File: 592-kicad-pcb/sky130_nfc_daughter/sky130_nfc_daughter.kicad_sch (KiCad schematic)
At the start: 57 parts, among them J1 U.FL, J2 U.FL, J3 U.FL, J4 U.FL, J5 U.FL, J6 U.FL, J7 U.FL, U1 Caravel_QFN, U3 W25Q32JVZP

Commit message: Add files via upload
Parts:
- removed C10: 0.1uf, Capacitor_SMD:C_0402_1005Metric, symbol Device:C
- removed C15, C16, C17, C3: C_1u_0603_50V, Capacitor_SMD:C_0603_1608Metric, symbol psypassives:C_1u_0603_50V
- removed R3, R4: 0R, Resistor_SMD:R_1206_3216Metric, symbol Device:R
- added C10, C20, C21, C23: C_1u_0603_50V, Capacitor_SMD:C_0603_1608Metric, symbol psypassives:C_1u_0603_50V
- added C22, C3: 0.1uf, Capacitor_SMD:C_0402_1005Metric, symbol Device:C
- added JP10, JP11, JP6, JP7, JP8, JP9: Jumper_2_Small_Bridged, Jumper:SolderJumper-2_P1.3mm_Bridged_RoundedPad1.0x1.5mm, symbol Jumper:Jumper_2_Small_Bridged
- added R1: 10k, Resistor_SMD:R_0402_1005Metric, symbol Device:R
- added TP5: TestPoint_Alt, TestPoint:TestPoint_Keystone_5019_Minature, symbol Connector:TestPoint_Alt
- TP1, TP2, TP3, TP4: now fitted
- TP6: renamed from TP9; now fitted
- renumbered JP13 to JP2, JP2 to JP5
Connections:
- net GND: now also CON1.17 (Pin_17), C10.2, C20.2, C21.2, C22.2, C23.1, C3.1; no longer CON1.27 (Pin_27), CON1.33 (Pin_33)
- net VDD_EXT: now also C22.1, C23.2, JP11.2 (B), TP5.1; no longer CON1.39 (Pin_39)
- net ext_clk_dig: now also J3.1, JP5.1 (A)
- net ext_reset_dig: no longer J3.1, JP5.1 (A)
- net flash_csb: now also R1.2
- net gpio_0_0: now also CON1.19 (Pin_19)
- net gpio_1_0: now also CON1.21 (Pin_21)
- net at CON1.14 (Pin_14): now also JP10.1 (A)
- net flash_wpb: now reaches R9.2, U3.3 (~{WP}/IO_{2})
- net flash_rstb: now reaches R10.2, U3.7 (~{HOLD}/~{RESET}/IO_{3})
- net vccd_all renamed vccd_user_1v8
- net vccd_user_1v8: now also TP3.1, JP9.1 (A); no longer C2.1, C4.2, TP2.1, U1.18 (vccd)
- net vccd_in: no longer names the net of CON1.7 (Pin_7)
- net vccd_in: no longer TP4.1
- net vdda_all renamed vdda_user_3v3
- net vdda_user_3v3: now also TP4.1, C20.1, C21.1, JP10.2 (B), JP8.1 (A); no longer R10.1, R9.1, TP1.1, U1.30 (vdda), U3.8 (VCC)
- net vdda_in: no longer names the net of CON2.2 (Pin_2)
- net vdda_in: now also JP6.1 (A); no longer TP3.1
- net vddio renamed vddio_vdda_mgmt_3v3
- net vddio_vdda_mgmt_3v3: now also R10.1, R9.1, TP2.1, U1.30 (vdda), U3.8 (VCC), C3.2, JP7.2 (B), R1.1; no longer CON2.4 (Pin_4)
- new net: CON1.27 (Pin_27), JP8.2 (B)
- new net: CON1.33 (Pin_33), JP9.2 (B)
- new net: CON1.39 (Pin_39), JP11.1 (A)
- new net: CON2.4 (Pin_4), JP7.1 (A)
- new net vccd_mgmt_1v8: C10.1, C2.1, C4.2, JP6.2 (B), TP1.1, U1.18 (vccd)
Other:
- note added: "ADD RESET BUTTON"
- note added: "PWR/GND probes"
- note removed: "Bidir[0..1]"
- note removed: "GND probe point"
- note removed: "Input (7 below)"
- note removed: "Replace 0R with current sense resistors to monitor current on rail"
- moved on the sheet: C1, C11, C12, C13, C14, C18, C19, C4, C5, C6, C7, C8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

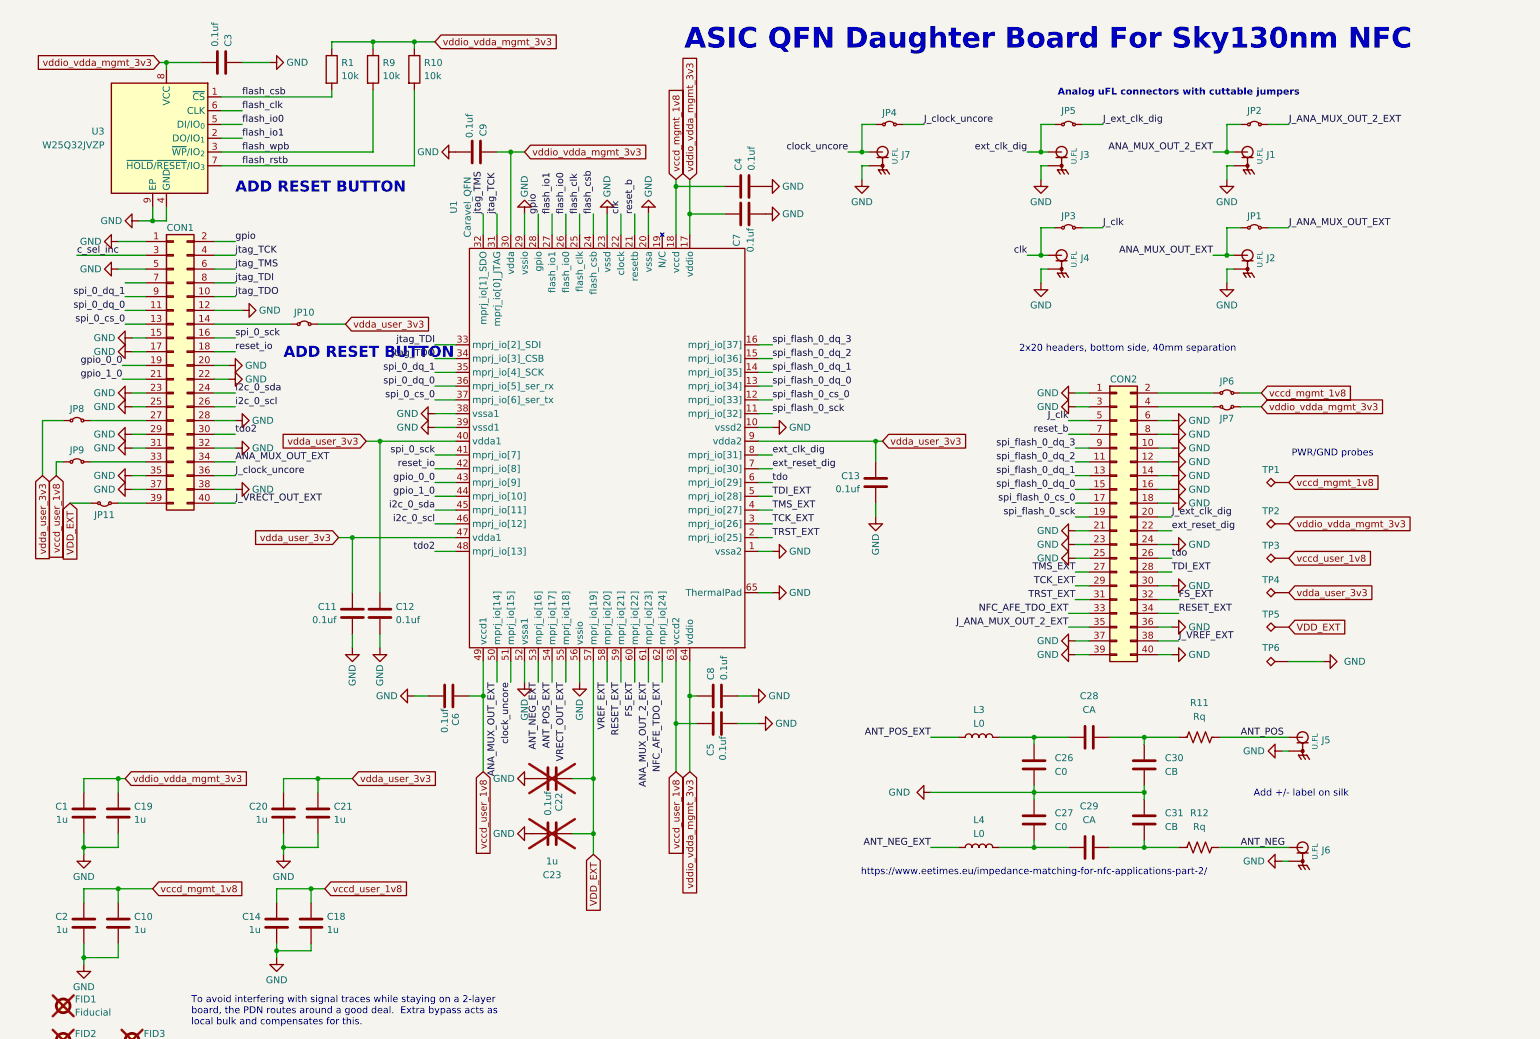
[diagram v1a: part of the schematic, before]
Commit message: add mezzanine symbol/footprint, init daughterboard placement
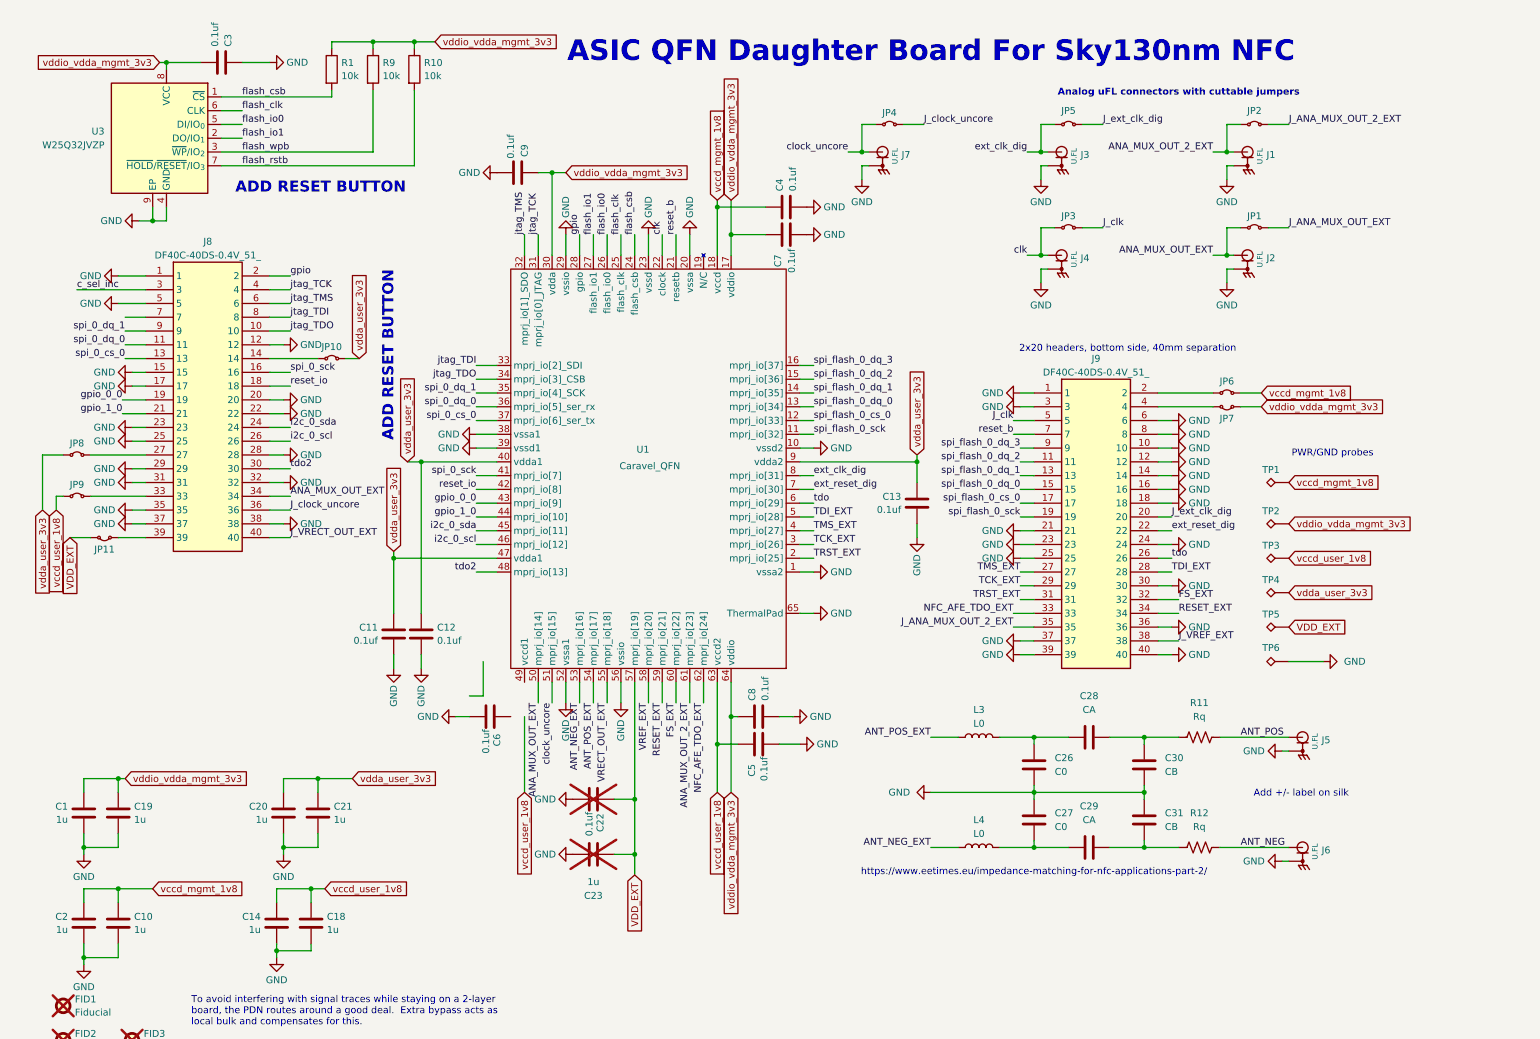
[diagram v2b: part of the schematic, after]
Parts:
- removed CON1, CON2: ~, TinyTapeout:FH-00148_PinSocket_2x20_P2.54mm, symbol Connector_Generic:Conn_02x20_Odd_Even
- added J8, J9: DF40C-40DS-0.4V_51_, 592-partslib:DF40C40DS04V51, symbol 592-partslib:DF40C-40DS-0.4V_51_
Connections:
- net ANA_MUX_OUT_EXT: now also J8.34
- net FS_EXT: now also J9.32
- net GND: now also J8.1, J8.12, J8.15, J8.17, J8.20, J8.22, J8.23, J8.25, J8.28, J8.29, J8.31, J8.32, J8.35, J8.37, J8.38, J8.5, J9.1, J9.10, J9.12, J9.14, J9.16, J9.18, J9.21, J9.23, J9.24, J9.25, J9.3, J9.30, J9.36, J9.37, J9.39, J9.40, J9.6, J9.8
- net J_ANA_MUX_OUT_2_EXT: now also J9.35
- net J_VRECT_OUT_EXT: now also J8.40
- net J_VREF_EXT: now also J9.38
- net J_clk: now also J9.5
- net J_clock_uncore: now also J8.36
- net J_ext_clk_dig: now also J9.20
- net NFC_AFE_TDO_EXT: now also J9.33
- net RESET_EXT: now also J9.34
- net TCK_EXT: now also J9.29
- net TDI_EXT: now also J9.28
- net TMS_EXT: now also J9.27
- net TRST_EXT: now also J9.31
- net c_sel_inc: now also J8.3
- net ext_reset_dig: now also J9.22
- net gpio: now also J8.2
- net gpio_0_0: now also J8.19
- net gpio_1_0: now also J8.21
- net i2c_0_scl: now also J8.26
- net i2c_0_sda: now also J8.24
- net jtag_TCK: now also J8.4
- net jtag_TDI: now also J8.8
- net jtag_TDO: now also J8.10
- net jtag_TMS: now also J8.6
- net reset_b: now also J9.7
- net reset_io: now also J8.18
- net spi_0_cs_0: now also J8.13
- net spi_0_dq_0: now also J8.11
- net spi_0_dq_1: now also J8.9
- net spi_0_sck: now also J8.16
- net spi_flash_0_cs_0: now also J9.17
- net spi_flash_0_dq_0: now also J9.15
- net spi_flash_0_dq_1: now also J9.13
- net spi_flash_0_dq_2: now also J9.11
- net spi_flash_0_dq_3: now also J9.9
- net spi_flash_0_sck: now also J9.19
- net tdo: now also J9.26
- net tdo2: now also J8.30
- net vccd_user_1v8: no longer C6.1, U1.49 (vccd1)
- net at JP10.1 (A): now also J8.14
- net at JP8.2 (B): now also J8.27
- net at JP9.2 (B): now also J8.33
- net at JP11.1 (A): now also J8.39
- net at JP7.1 (A): now also J9.4
- net at JP6.1 (A): now also J9.2
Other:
- moved on the sheet: C11, C12, C13, C22, C23, C4, C5, C6, C7, C8, C9, JP10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

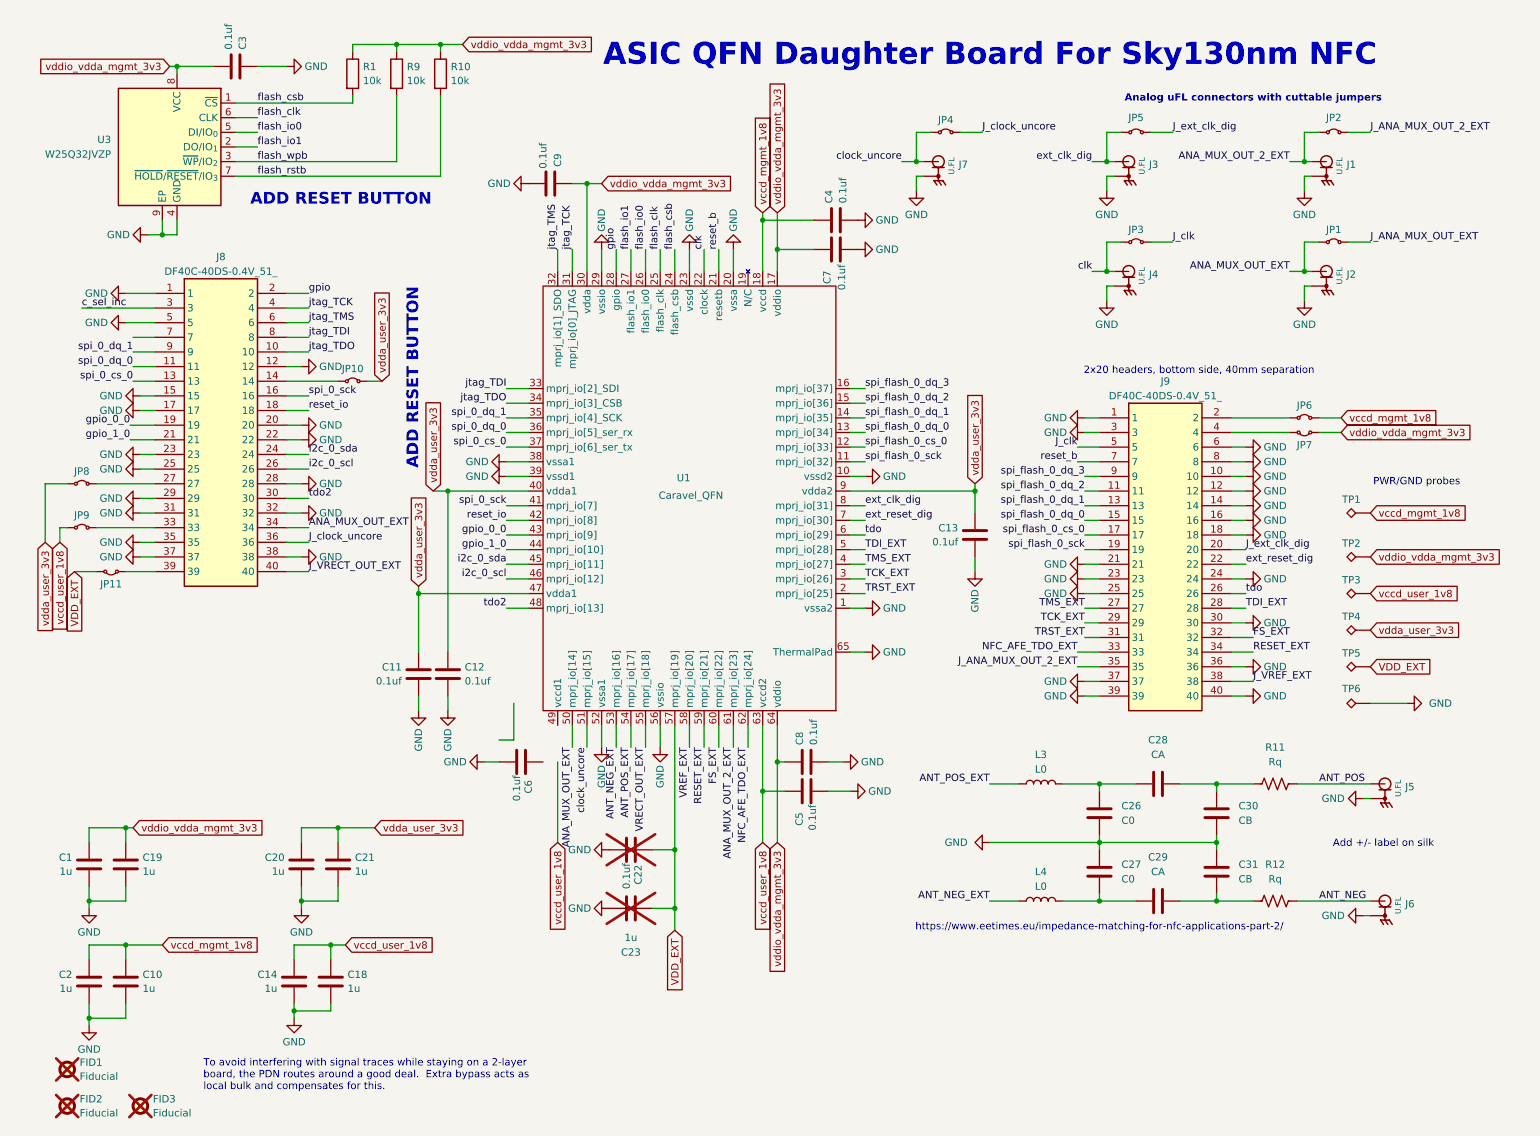
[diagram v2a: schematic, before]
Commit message: daughter placement v1, add 3D models for mezzanine + uFL
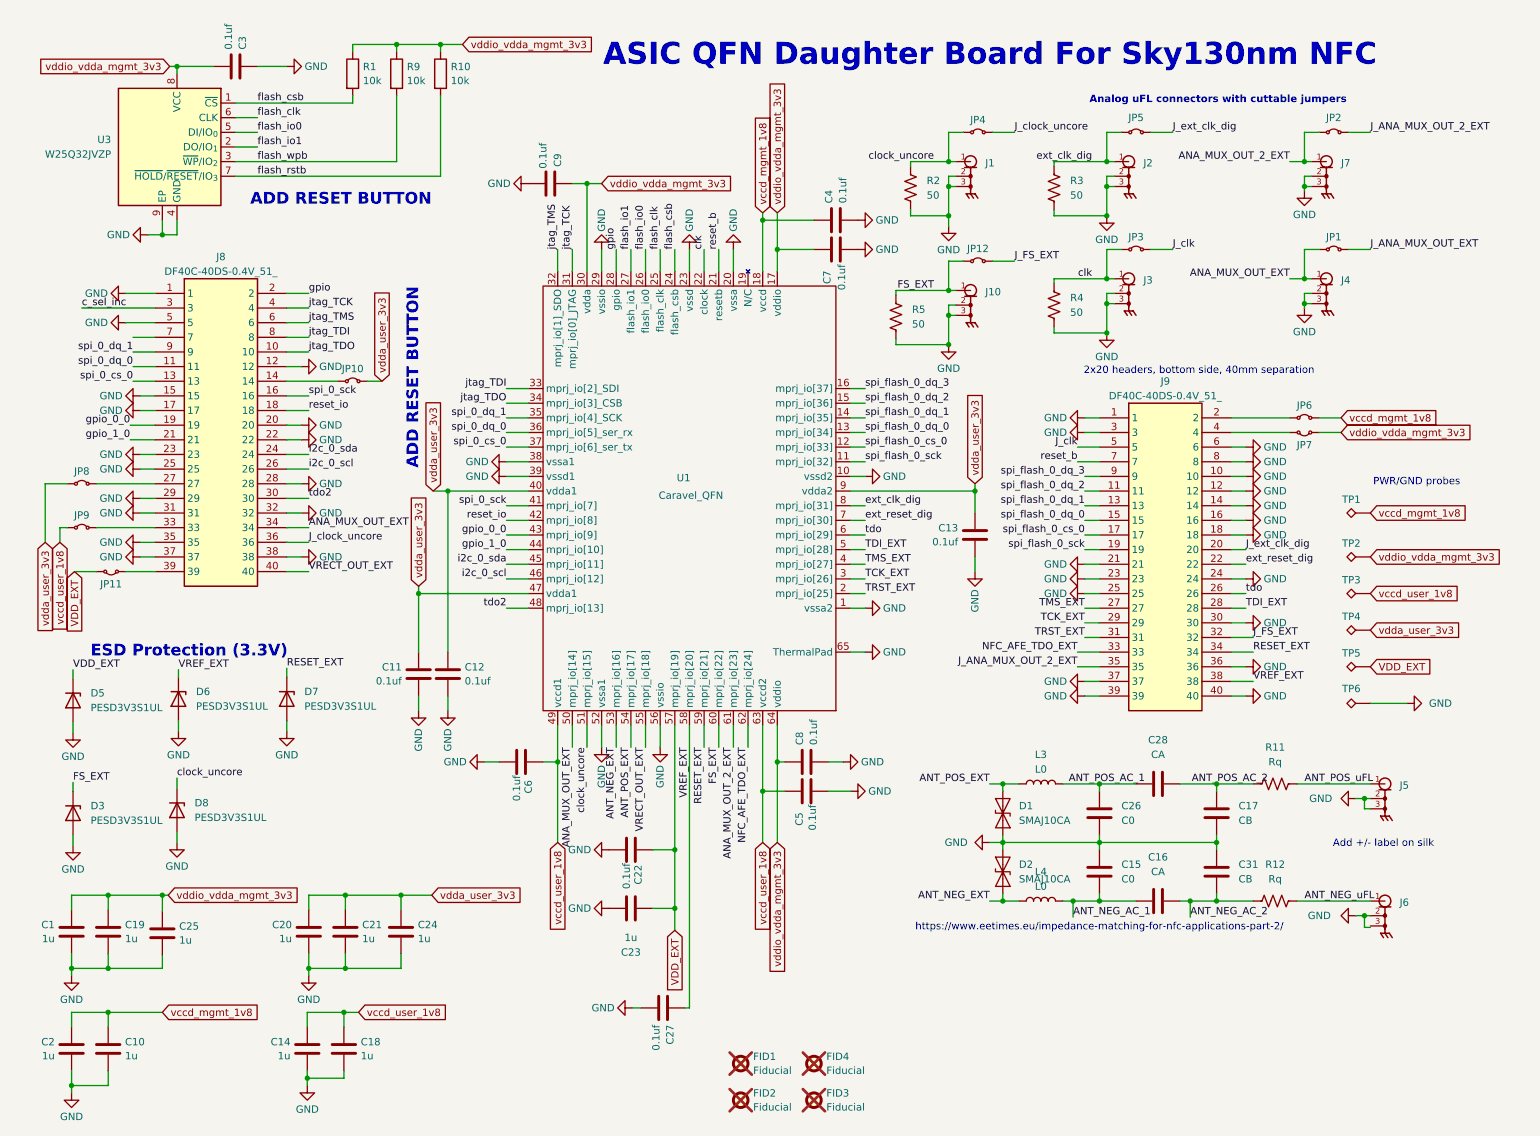
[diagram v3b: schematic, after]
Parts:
- removed C29: CA, symbol Device:C
- removed C30: CB, symbol Device:C
- removed J1, J2, J3, J4, J5, J6, J7: U.FL, psysnapeda:SAMTEC_RSP-122811-01, symbol psysnapeda:RSP-122811-01
- added C15: C0, Capacitor_SMD:C_0603_1608Metric_Pad1.08x0.95mm_HandSolder, symbol Device:C
- added C16: CA, Capacitor_SMD:C_0603_1608Metric_Pad1.08x0.95mm_HandSolder, symbol Device:C
- added C17: CB, Capacitor_SMD:C_0603_1608Metric_Pad1.08x0.95mm_HandSolder, symbol Device:C
- added C24, C25: C_1u_0603_50V, Capacitor_SMD:C_0603_1608Metric, symbol psypassives:C_1u_0603_50V
- added D1, D2: SMAJ10CA, Diode_SMD:D_SMA, symbol Diode:SMAJ10CA
- added D3, D5, D6, D7, D8: PESD3V3S1UL, Diode_SMD:D_SOD-882, symbol Diode:PESD3V3S1UL
- added FID4: Fiducial, Fiducial:Fiducial_1mm_Mask2mm, symbol Mechanical:Fiducial
- added J1, J10, J2, J3, J4, J5, J6, J7: U.FL-R-SMT-1_80_, 592-partslib:UFLRSMT180, symbol 592-partslib:U.FL-R-SMT-1_80_
- added JP12: Jumper_2_Small_Bridged, Jumper:SolderJumper-2_P1.3mm_Bridged_RoundedPad1.0x1.5mm, symbol Jumper:Jumper_2_Small_Bridged
- added R2, R3, R4, R5: 50, Resistor_SMD:R_0402_1005Metric, symbol Device:R_US
- C22, C23: now fitted
- C26, C28, C31: footprint (none) -> Capacitor_SMD:C_0603_1608Metric_Pad1.08x0.95mm_HandSolder
- C27: value C0 -> 0.1uf; footprint (none) -> Capacitor_SMD:C_0402_1005Metric; Characteristics (none) -> 100n 0402; LCSC (none) -> C100072; MPN (none) -> CL05A104KA5NNNC; MPN_ALT (none) -> GRM155R71E104KE14J
- L3, L4: footprint (none) -> Inductor_SMD:L_0603_1608Metric_Pad1.05x0.95mm_HandSolder
- R11, R12: footprint (none) -> Resistor_SMD:R_0603_1608Metric_Pad0.98x0.95mm_HandSolder
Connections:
- net J_VRECT_OUT_EXT is gone; now on net VRECT_OUT_EXT: J8.40
- net J_VREF_EXT is gone; now on net VREF_EXT: J9.38
- net ANA_MUX_OUT_2_EXT: now also J7.1
- net ANA_MUX_OUT_EXT: now also J4.1
- net ANT_NEG_EXT: now also D2.2 (A2)
- net ANT_POS_EXT: now also D1.2 (A2)
- net FS_EXT: now also D3.1 (K), J10.1, JP12.1 (A), R5.2; no longer J9.32
- net GND: now also C27.2, C15.1, C17.2, C24.2, C25.2, D1.1 (A1), D2.1 (A1), D3.2 (A), D5.2 (A), D6.2 (A), D7.2 (A), D8.2 (A), J1.2, J1.3, J10.2, J10.3, J2.2, J2.3, J3.2, J3.3, J4.2, J4.3, J5.2, J5.3, J6.2, J7.2, J7.3, R2.1, R3.1, R4.1, R5.1; no longer C27.1
- net RESET_EXT: now also D7.1 (K)
- net VDD_EXT: now also D5.1 (K)
- net VREF_EXT: now also C27.1, D6.1 (K)
- net clk: now also J3.1, R4.2
- net clock_uncore: now also D8.1 (K), J1.1, R2.2
- net ext_clk_dig: now also J2.1, R3.2
- net vccd_user_1v8: now also C6.1, U1.49 (vccd1)
- net vdda_user_3v3: now also C24.1
- net vddio_vdda_mgmt_3v3: now also C25.1
- net ANT_NEG_AC_1: now reaches L4.2
- net ANT_NEG_AC_1: now also C15.2, C16.1; no longer C27.2
- net ANT_NEG_AC_2: now reaches C31.2, R12.1
- net ANT_NEG_AC_2: now also C16.2
- net ANT_POS_AC_2: now reaches C28.2, R11.1
- net ANT_POS_AC_2: now also C17.1
- net ANT_POS_AC_1: now reaches C26.1, C28.1, L3.2
- net ANT_NEG renamed ANT_NEG_uFL
- net ANT_NEG_uFL: now also J6.1
- net ANT_POS renamed ANT_POS_uFL
- net ANT_POS_uFL: now also J5.1
- new net J_FS_EXT: J9.32, JP12.2 (B)
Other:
- note added: "ESD Protection (3.3V)"
- note removed: "To avoid interfering with signal traces while staying on a 2-layer board, the PDN routes around a good deal. Extra bypass acts as local bulk and compensates for this."
- moved on the sheet: C1, C10, C14, C18, C19, C2, C20, C21, FID1, FID2, FID3, JP1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
